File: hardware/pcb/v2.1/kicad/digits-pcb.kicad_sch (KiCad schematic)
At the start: 45 parts, among them J1 Conn_02x20_Odd_Even, J3 VIN_BARREL_PIGTAIL, J4 Conn_01x07, J6 Conn_01x02, J7 Screw_Terminal_01x02, J8 Conn_01x04, J9 Conn_01x03, SW1 SW_Push, U1 LM2596S-5, U3 RP2040, U4 W25Q16JVSSIQ, U5 AMS1117-3.3, Y1 ABM8-272-T3

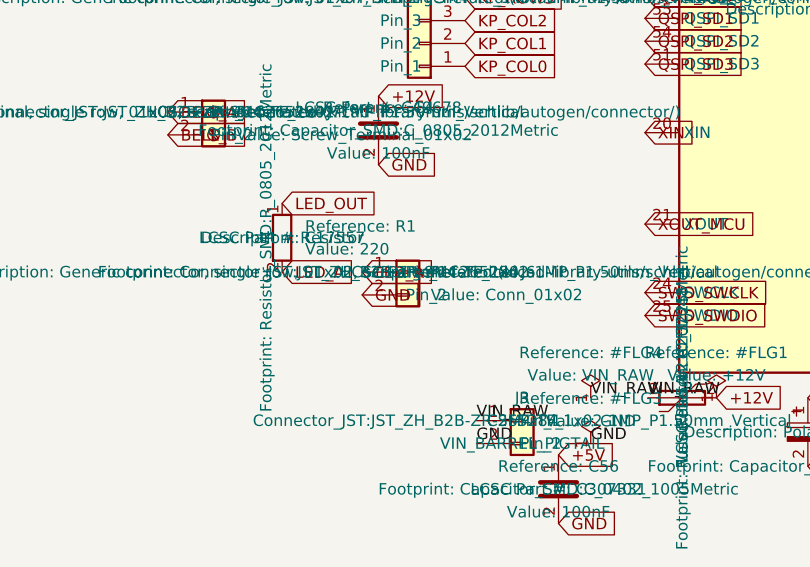
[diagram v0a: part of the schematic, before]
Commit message: fix(hardware): swap V2.1 J6 LED pin polarity to match stock pigtail
V2 wired J6 with pin 1 = LED anode (through R1 from GPIO16) and
pin 2 = GND. The stock LED pigtail crimps the opposite polarity at
the JST end, back-biasing the LED on plug-in and leaving it dark.
Same class of defect as the J8 handset-cable issue: a connector
polarity adopted without an explicit wire-to-pin assertion against
a physical cable.

V2.1 now has J6.1 = GND and J6.2 = LED_A (driven through R1).
Schematic change is two global-label text swaps; PCB re-route is
two short nets around J6 (GPIO16 side unchanged).

V1 has the same defect and is documented in V1 ERRATA entry #5
(separate PR). V2 fabbed boards should re-crimp the pigtail.
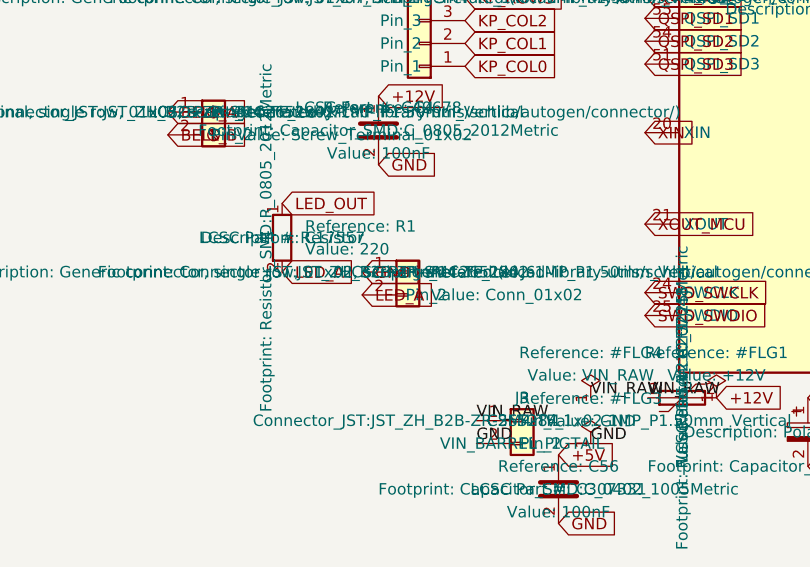
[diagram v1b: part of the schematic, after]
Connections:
- net GND: now also J6.1 (Pin_1); no longer J6.2 (Pin_2)
- net LED_A: now also J6.2 (Pin_2); no longer J6.1 (Pin_1)
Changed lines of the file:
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@@
     )
   )
-  (global_label "LED_A" (shape input) (at 43.18 125.73 0)
+  (global_label "GND" (shape input) (at 43.18 125.73 0)
     (effects (font (size 1.27 1.27)) (justify left))
     (property "Intersheetrefs" "${INTERSHEET_REFS}" (at 43.18 125.73 0) (show_name)
@@
     )
   )
-  (global_label "GND" (shape input) (at 43.18 128.27 0)
+  (global_label "LED_A" (shape input) (at 43.18 128.27 0)
     (effects (font (size 1.27 1.27)) (justify left))
     (property "Intersheetrefs" "${INTERSHEET_REFS}" (at 43.18 128.27 0) (show_name)
